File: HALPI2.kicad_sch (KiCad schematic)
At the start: 17 parts

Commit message: Weeded out all ERC errors
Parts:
- removed FID1, FID2, FID3, FID4, FID5, FID6, FID7, FID8: Fiducial, Fiducial:Fiducial_1mm_Mask2mm, symbol Mechanical:Fiducial
- removed H1, H2, H3, H4: MountingHole, MountingHole:MountingHole_2.7mm_M2.5, symbol Mechanical:MountingHole
- removed H101, H102, H5, H6: MountingHole, Yellow:DrillSlot_Plated_3.5x2.5mm, symbol Mechanical:MountingHole
- removed HS1: Heatsink, Yellow:Heatsink_56x56mm_2xFixation3.2mm, symbol Mechanical:Heatsink
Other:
- added sheet PCB (pcb.kicad_sch)
- added sheet USB3 (USB3.kicad_sch)
- sheet CM4 GPIO ports: added CAM_GPIO0, CAM_GPIO1, FAN_PWM, FAN_TACHO, ID{I2C}, PWR_BUTTON, RS485{UART}, VBAT, {OTG_USB}; removed CM4_DBG{TX RX}, PCIe{PCIe}, RESET_CM4, RS-485{UART}, {CM4_USB}, ~{EXTRST}, ~{FAN_PWM}
- sheet CM4 Highspeed ports: added CAM_GPIO0, CAM_GPIO1, I2C0{I2C}, ID{I2C}, PCIe{PCIe}, USB3-0{USB3}, USB3-1{USB3}, VBUS_EN, {OTG_USB}; removed none
- sheet Control - RTC ports: added FAN_PWM, FAN_TACHO, VBAT; removed ~{FAN_PWM}, ~{LED_ACT}, ~{LED_PWR}
- sheet Controller ports: added PWR_BTN_OUT; removed none
- sheet PoE ports: added Vcap, Vin_prot; removed DC_IN_F
- sheet Power ports: added none; removed DC_IN_F
- sheet USB ports: added {OTG_USB}; removed CM4_DBG{TX RX}, {CM4_USB}, ~{EXTRST}, ~{RESET_CM4}
- note added: "Connectors ------- 40way RPI Jumpers"
- note added: "Connectors ------- HDMI 0 HDMI 1 DPHY 0 DPHY 1"
- note removed: "Connectors ------- Ethernet SDCARD 40way RPI Jumpers"
- note removed: "Connectors ------- HDMI 0 HDMI 1 CSI 0 CSI 1 DSI 0 DSI 1"
- company: Nabu Casa -> Hat Labs Oy
- title: Overview -> HALPI2

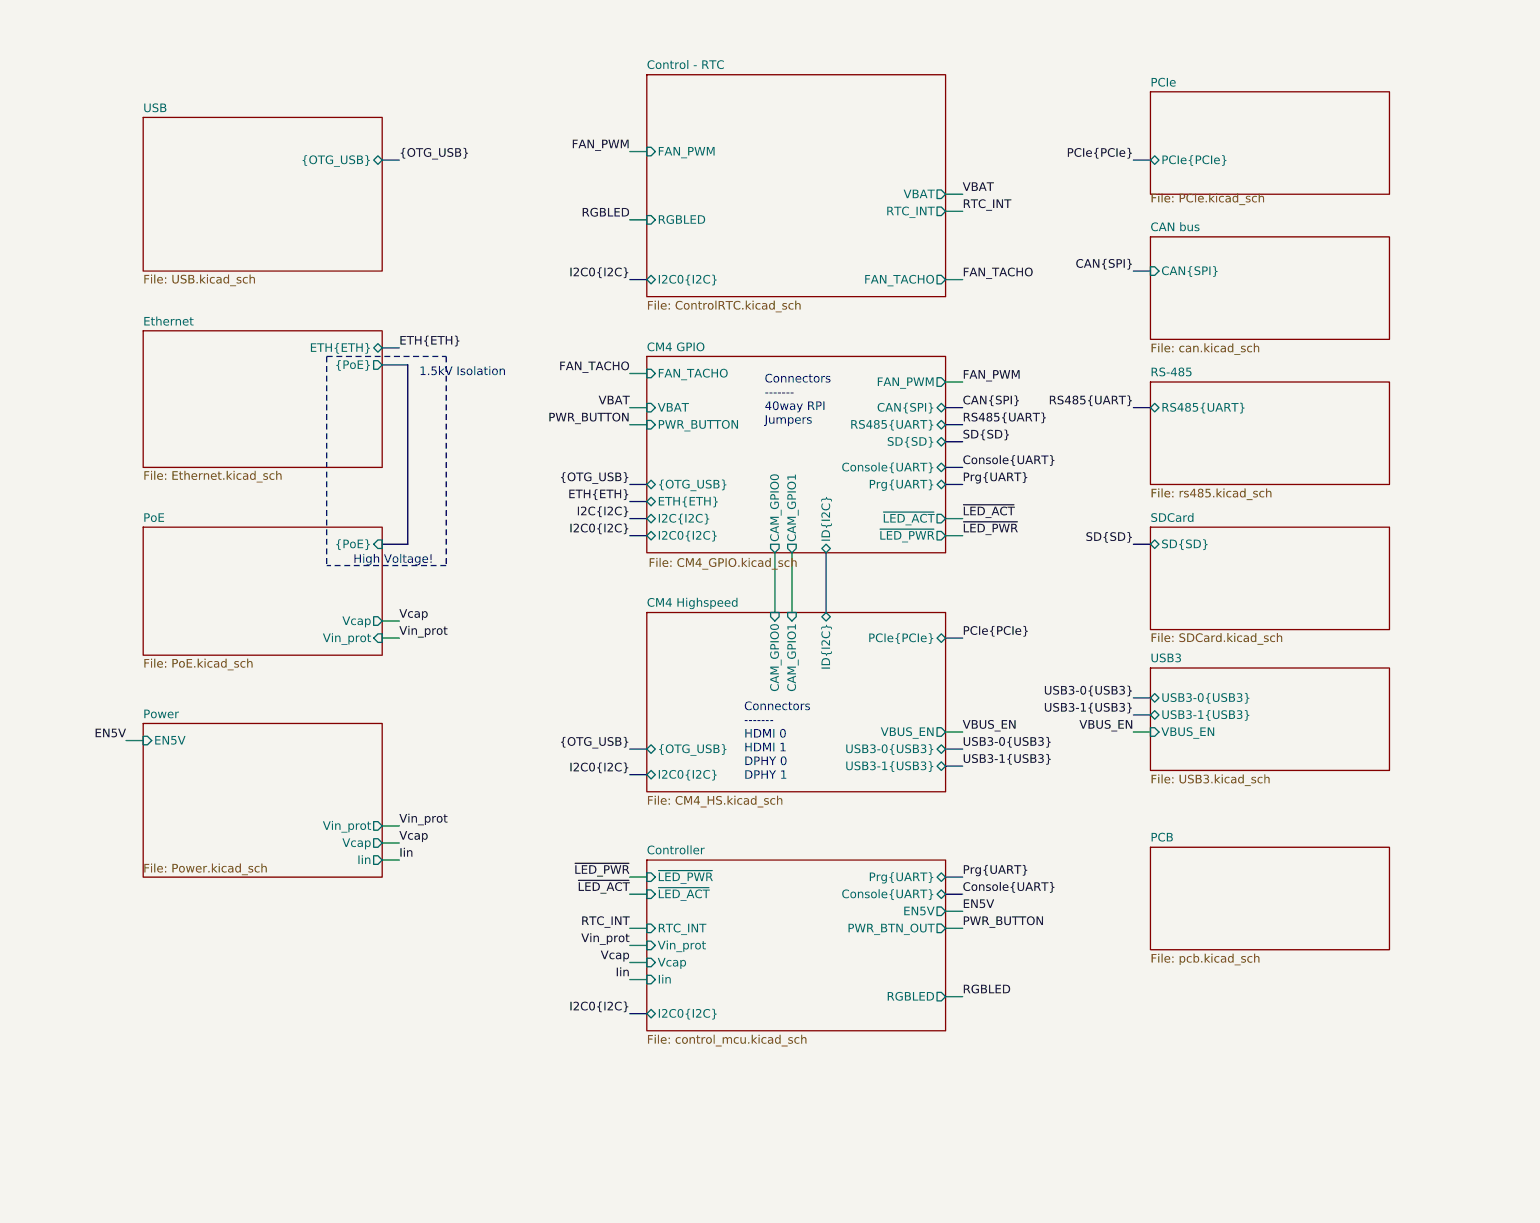
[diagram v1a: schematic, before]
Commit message: Implement ideal diodes for input and LDO power ORing
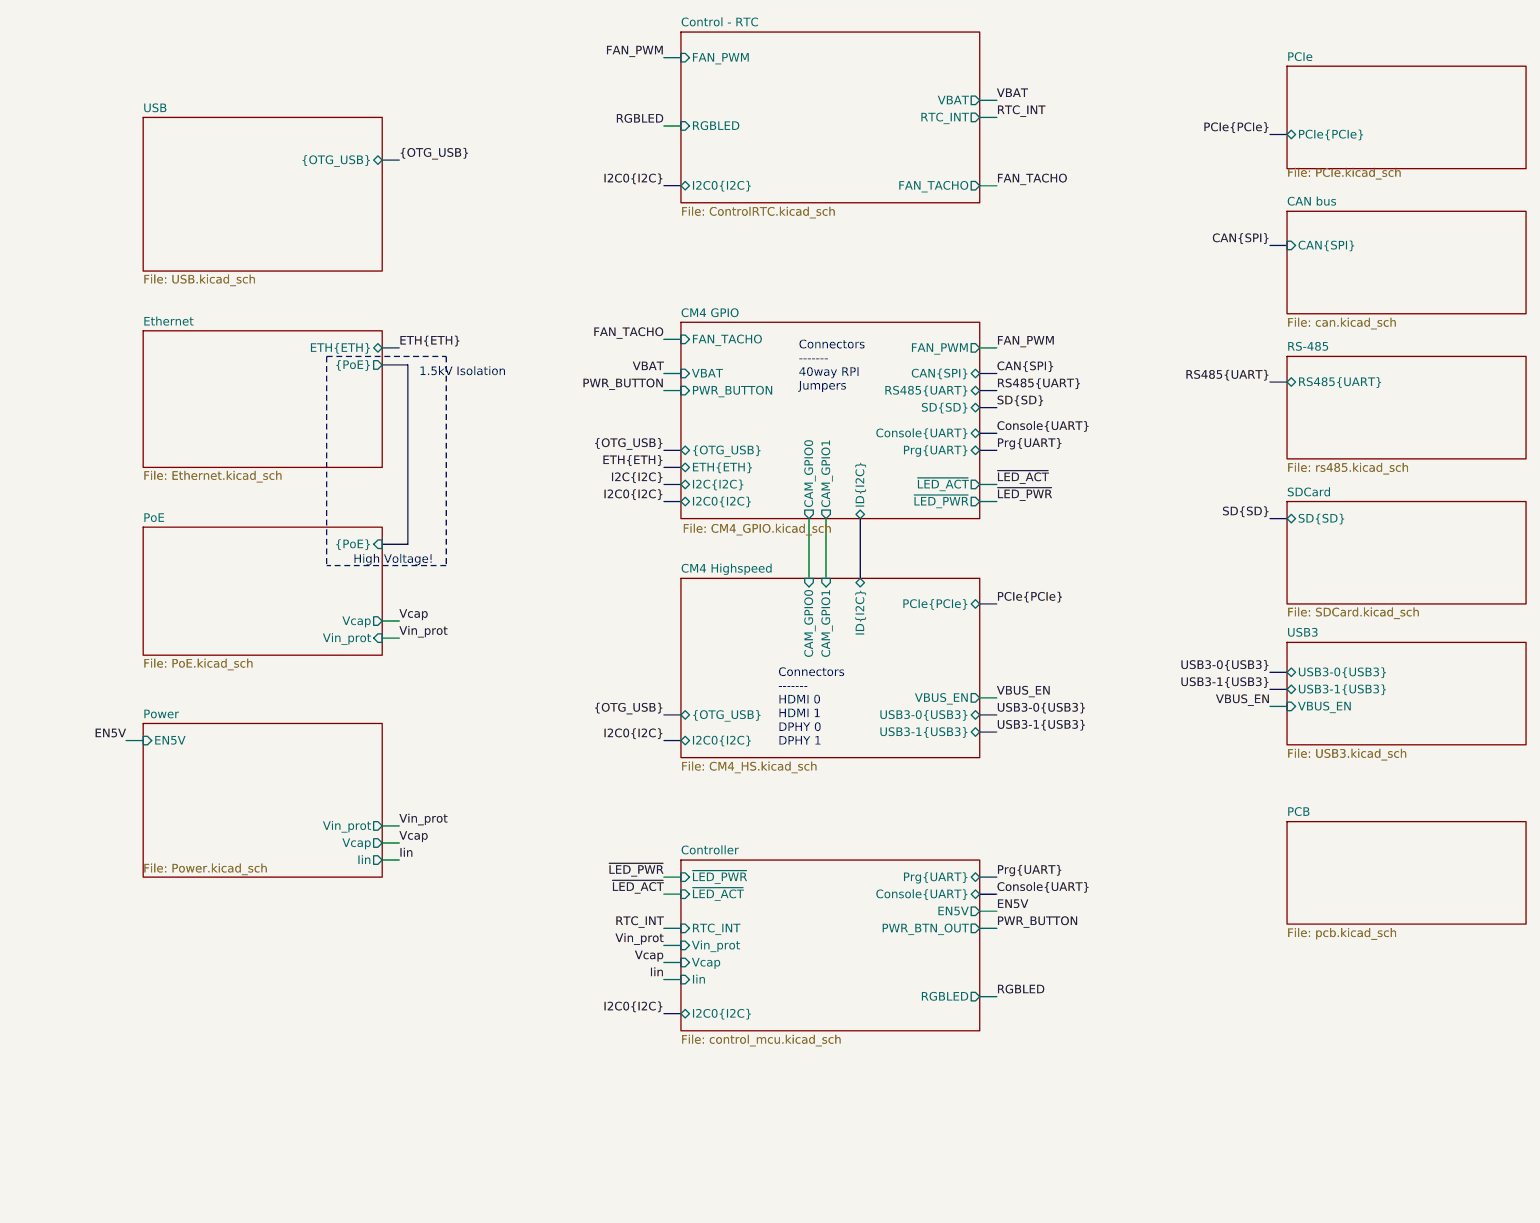
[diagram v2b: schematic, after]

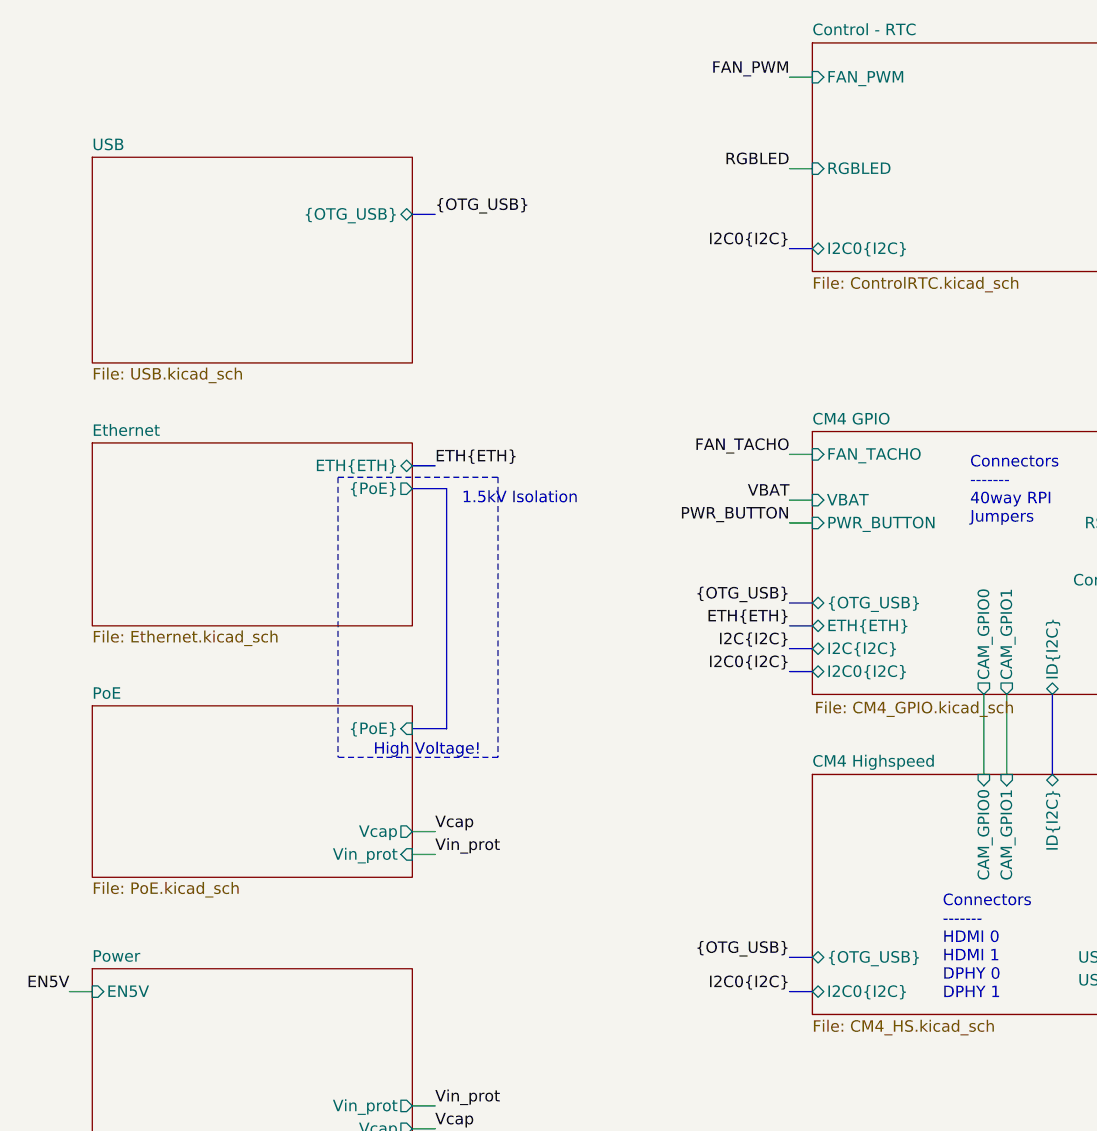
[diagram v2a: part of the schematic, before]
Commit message: Implement a USB3 hub
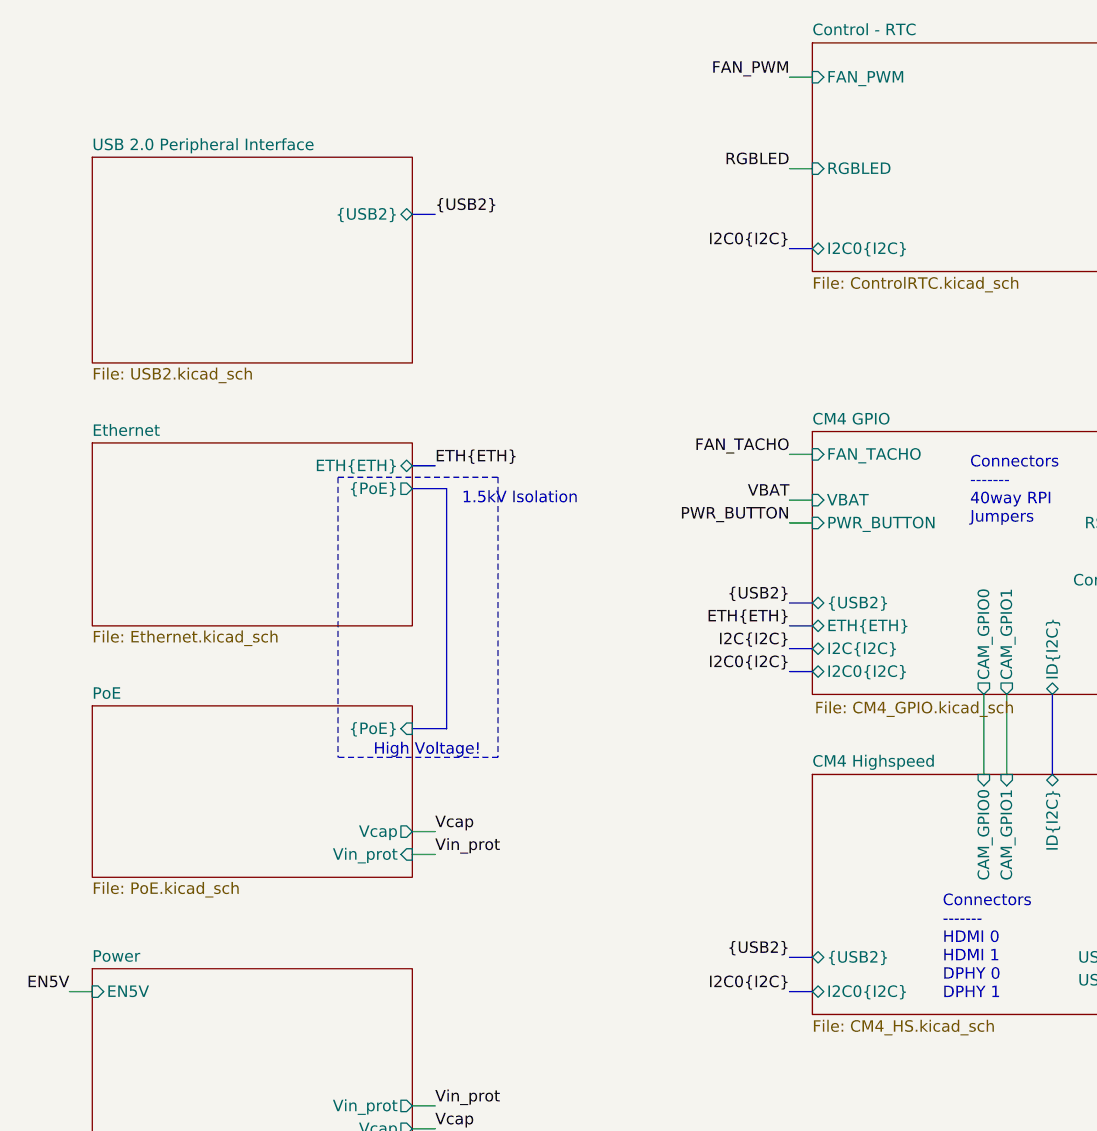
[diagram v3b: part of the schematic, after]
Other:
- sheet USB renamed USB 2.0 Peripheral Interface
- sheet CM4 GPIO ports: added {USB2}; removed {OTG_USB}
- sheet CM4 Highspeed ports: added {USB2}; removed {OTG_USB}
- sheet USB 2.0 Peripheral Interface: file USB.kicad_sch -> USB2.kicad_sch
- sheet USB 2.0 Peripheral Interface ports: added {USB2}; removed {OTG_USB}
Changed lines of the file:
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@@
 		)
 	)
-	(label "{OTG_USB}"
+	(label "{USB2}"
 		(at 113.03 119.38 180)
 		(fields_autoplaced yes)
@@
 		)
 	)
-	(label "{OTG_USB}"
+	(label "{USB2}"
 		(at 73.66 36.83 0)
 		(fields_autoplaced yes)
@@
 		)
 	)
-	(label "{OTG_USB}"
+	(label "{USB2}"
 		(at 113.03 80.01 180)
 		(fields_autoplaced yes)
@@
 			)
 		)
-		(pin "{OTG_USB}" bidirectional
+		(pin "{USB2}" bidirectional
 			(at 115.57 80.01 180)
 			(effects
@@
 			)
 		)
-		(pin "{OTG_USB}" bidirectional
+		(pin "{USB2}" bidirectional
 			(at 115.57 119.38 180)
 			(effects
@@
 			(color 255 255 255 0.0000)
 		)
-		(property "Sheetname" "USB"
+		(property "Sheetname" "USB 2.0 Peripheral Interface"
 			(at 35.56 29.8441 0)
 			(effects
@@
 			)
 		)
-		(property "Sheetfile" "USB.kicad_sch"
+		(property "Sheetfile" "USB2.kicad_sch"
 			(at 35.56 53.8489 0)
 			(effects
@@
 			)
 		)
-		(pin "{OTG_USB}" bidirectional
+		(pin "{USB2}" bidirectional
 			(at 71.12 36.83 0)
 			(effects
